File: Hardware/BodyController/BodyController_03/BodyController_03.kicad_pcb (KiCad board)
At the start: 4 copper layers, 155 x 106 mm, 401 parts, among them J1 7796, J10 Conn_01x01, J11 Conn_01x01, J12 Conn_01x01, J13 Conn_01x01, J14 TEST_1P, J15 TEST_1P, J16 TEST_1P, J17 TEST_1P, J18 TEST_1P, J2 Conn_01x14, J3 Conn_02x10_Top_Bottom, J4 Conn_02x10_Top_Bottom, J5 7796, J6 7796, J7 CONN_01X06, J8 USB_OTG, J9 Conn_01x01, Q1 NX1029X,115, Q10 NX1029X,115, Q12 BUK9Y3R0-40E,115, Q13 BUK9Y3R0-40E,115, Q16 2N7002, Q17 Q_PMOS_GSD, Q2 NX1029X,115, Q3 2N7002, Q4 SQJ423EP-T1_GE3, Q6 NX1029X,115, Q7 NX1029X,115, Q8 2N7002, Q9 2N7002, SW1 PTS645SM43SMTR92 LFS, U1 PIC33EPxxxMU810, U10 LM2904AVQDRQ1, U11 BTS50202EKAXUMA2, U12 BTS50202EKAXUMA2, U13 BTS50202EKAXUMA2, U15 BTS716G, U16 MCP2562-H/SN, U17 TPS70950QDBVRQ1, U18 TPS70933QDBVRQ1, U19 TPS70933QDBVRQ1, U2 LM2903QDRQ1, U20 LMR140x0, U21 LM2903QDRQ1, U22 DRV8872DDARQ1, U23 tps25940-q1, U25 UCC27511A-Q1, U27 INA21x, U29 FT230X, U3 INA21x, U4 BTS716G, U5 BTS500801TMAATMA1, U6 BTS500801TMAATMA1, U7 BTS50202EKAXUMA2, U8 BTS50202EKAXUMA2, U9 BTS50202EKAXUMA2, Y1 8MHz

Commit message: Added output files
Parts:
- removed J14, J15, J16, J17, J18: TEST_1P, Measurement_Points:Test_Point_Keystone_5019_Minature
- added TP1: TEST_1P, Measurement_Points:Test_Point_Keystone_5019_Minature, F.Cu at (73.8, 88.8)
- added TP2: TEST_1P, Measurement_Points:Test_Point_Keystone_5019_Minature, F.Cu at (103.8, 90.5)
- added TP3: TEST_1P, Measurement_Points:Test_Point_Keystone_5019_Minature, F.Cu at (137.0, 117.0)
- added TP4: TEST_1P, Measurement_Points:Test_Point_Keystone_5019_Minature, F.Cu at (105.5, 99.0)
- added TP5: TEST_1P, Measurement_Points:Test_Point_Keystone_5019_Minature, F.Cu at (119.8, 85.2)
- added TP6: TEST_1P, Measurement_Points:Test_Point_Keystone_5019_Minature, F.Cu at (169.2, 113.2)
- added TP7: TEST_1P, Measurement_Points:Test_Point_Keystone_5019_Minature, F.Cu at (176.0, 63.8)
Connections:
- U2 pad 5: Net-(U2-Pad5) -> +3.3VP
- U2 pad 6: Net-(U2-Pad6) -> GND
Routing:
- net +3.3VP: track 259.6 -> 263.5 mm, vias 22 -> 23
- net GND: track 940.4 -> 943.4 mm
- net Net-(R74-Pad1): track 66.5 -> 67.6 mm
- net CHARGER_CONTACTOR_OUT: track 25.5 -> 26.3 mm
- added copper zone on B.Cu, net +BATT
- added copper zone on B.Cu, net /TopLevel/DCDC/DCDC_SHUNT
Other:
- board text added: "12V_MAIN"
- board text added: "E_Moto Main Controller Rev_01"
- board text removed: "E-Moto Main Controller Rev_01"

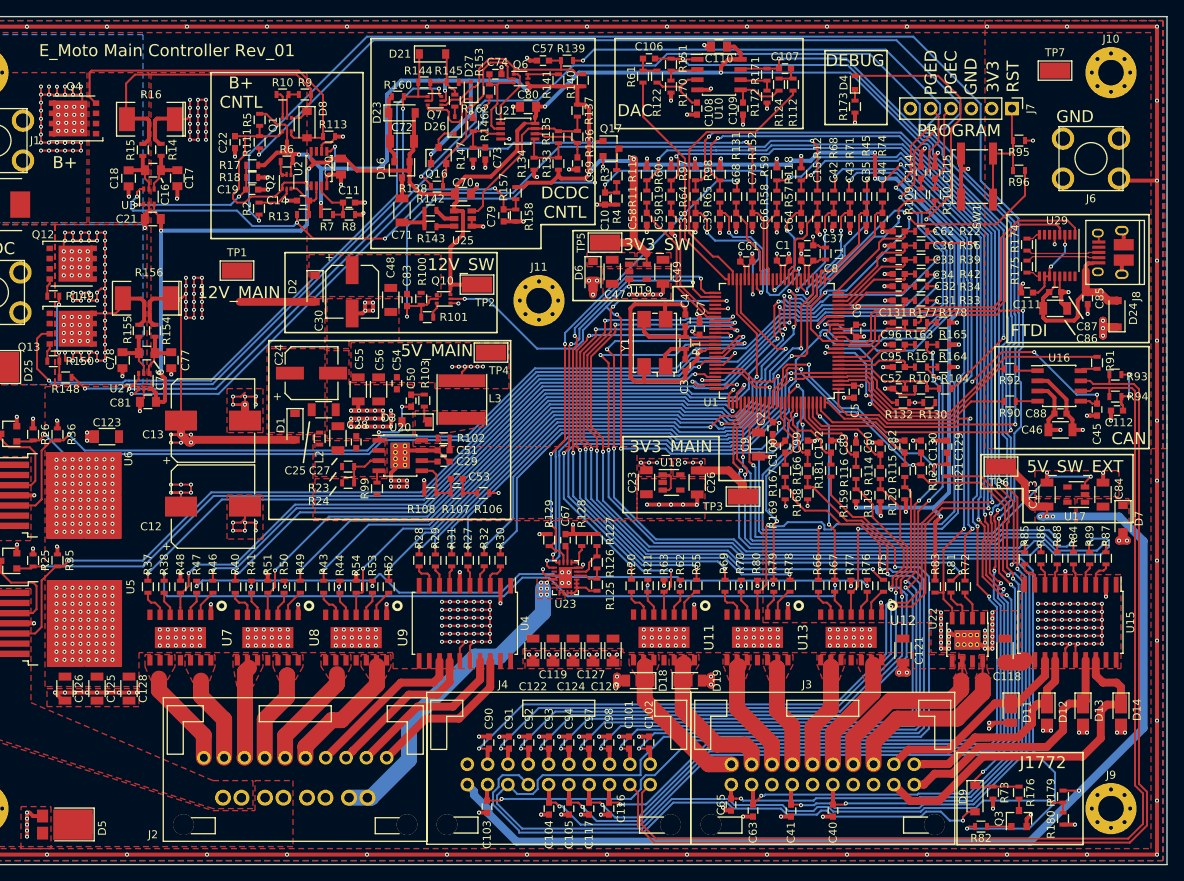
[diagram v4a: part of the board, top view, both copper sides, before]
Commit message: Added resistor values via BOM importer. Changed layout file to add large CAN resistors and buffer to 1.65V Reference
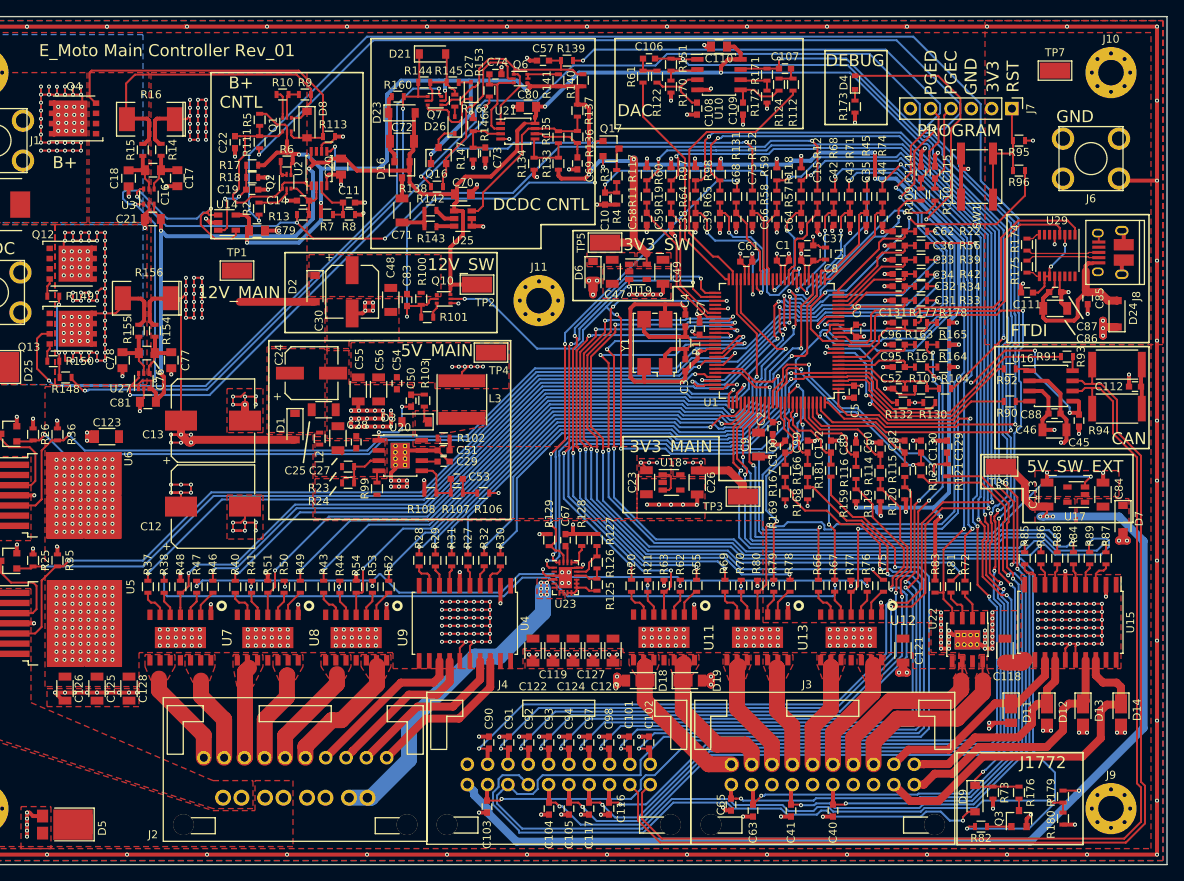
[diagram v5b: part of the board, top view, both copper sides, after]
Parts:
- removed R157, R158: 10k, Resistors_SMD:R_0603
- added U14: OPA320-Q1, TO_SOT_Packages_SMD:SOT-23-5, F.Cu at (72.5, 82.8)
- C79: value 10nF -> 1uF; footprint Capacitors_SMD:C_0603 -> Capacitors_SMD:C_0805
- R106: value 20 -> 20R
- R14, R149, R15, R150, R154, R155: value 3R -> 10R
- R142: value 1R -> 1R0
- R143: value 3R -> 3R0
- R147, R8: value 90k9 -> 100k
- R156: value R0005 -> R0003
- R16: value R -> R0005
- R93, R94: footprint Resistors_SMD:R_0603 -> Resistors_SMD:R_2512
- moved C79 30.9 mm to (76.2, 83.8), turned to 180 degrees
- moved R91 3.84 mm to (177.5, 99.5), turned to 180 degrees
- moved C112 3.75 mm to (186.0, 103.2)
- moved C45 2.65 mm to (179.0, 107.5)
- moved R94 1.51 mm to (183.8, 106.0)
- moved R93 1.27 mm to (183.8, 100.5)
- moved U16 1.02 mm to (175.5, 103.2)
- moved C46 0.75 mm to (175.9, 108.7)
- moved C88 0.75 mm to (175.9, 106.6)
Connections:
- C79 pad 1: Net-(C79-Pad1) -> GND
- C79 pad 2: GND -> +3.3VP
- U27 pad 1: Net-(C79-Pad1) -> 1V65_REF
- U3 pad 1: Net-(C19-Pad1) -> 1V65_REF
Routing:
- net Net-(C79-Pad1): track 63.2 -> 0.00 mm, vias 2 -> 0
- net 1V65_REF: track 0.00 -> 52.8 mm, vias 0 -> 3
- net +3.3VP: track 263.5 -> 275.2 mm, vias 23 -> 24
- net Net-(C19-Pad1): track 18.7 -> 11.1 mm
- net CAN_SLEEP: track 37.5 -> 33.0 mm
- net GND: track 943.4 -> 945.6 mm, vias 311 -> 312
- net Net-(C112-Pad1): track 7.60 -> 5.58 mm, vias 2 -> 0
- net Net-(R12-Pad1): track 103.0 -> 101.0 mm
- net CAN_P: track 134.8 -> 133.8 mm
- net Net-(R92-Pad1): track 2.82 -> 1.79 mm
- net Net-(R90-Pad1): track 2.74 -> 1.77 mm
- net Net-(R152-Pad1): track 108.6 -> 109.6 mm
- net CAN_N: track 132.3 -> 131.5 mm
